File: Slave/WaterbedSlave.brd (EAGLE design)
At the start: 53.2 x 50.4 mm, 8 parts

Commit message: Update WaterbedSlave.brd
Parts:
- added LED1: (no value), led:CHIPLED_0805
- added R1: 330, SparkFun-Resistors:0805
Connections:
- new net N$10: LED1.A, R1.1
- net GND: now also LED1.C
- net N$16: now also R1.2
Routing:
- net N$16: track 17.7 -> 21.1 mm
- net N$10: track 0.00 -> 2.45 mm
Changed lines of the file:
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@@
 <wire x1="0.2" y1="49.8" x2="0.4" y2="50" width="0.3048" layer="21"/>
 <text x="25.46" y="5.83" size="1.9304" layer="21" font="vector" ratio="13">Heat Pad</text>
-<text x="9.8" y="10.5" size="2.1844" layer="22" font="vector" ratio="13" rot="MR90">CuriousTech.net</text>
+<text x="8" y="11.2" size="2.1844" layer="22" font="vector" ratio="13" rot="MR90">CuriousTech.net</text>
 <text x="3" y="1.4" size="2.1844" layer="22" font="vector" ratio="13" rot="MR90">WiFi Waterbed Heater Slave</text>
 <text x="36.2" y="42.3" size="1.016" layer="21" font="vector" ratio="13">G 3v3 S</text>
@@
 <element name="JP2" library="SparkFun-Connectors" package="1X01_2MM" value="" x="38.4" y="3.9" rot="R180"/>
 <element name="F1" library="SparkFun-Capacitors" package="CAP-PTH-5MM" value="" x="22" y="14.3" rot="R90"/>
+<element name="LED1" library="led" package="CHIPLED_0805" value="" x="49.9" y="47.9" rot="R270"/>
+<element name="R1" library="SparkFun-Resistors" package="0805" value="330" x="45.6" y="47.8" rot="R180"/>
 </elements>
 <signals>
@@
 <contactref element="C1" pad="-"/>
 <contactref element="SUPP" pad="3V3"/>
+<contactref element="LED1" pad="C"/>
 </signal>
 <signal name="N$9">
@@
 <wire x1="48.268" y1="34.19" x2="49.586" y2="34.19" width="1.016" layer="1"/>
 <wire x1="49.586" y1="34.19" x2="49.134" y2="34.142" width="1.016" layer="1"/>
+<contactref element="R1" pad="2"/>
+<wire x1="44.7" y1="47.8" x2="41.812" y2="47.8" width="0.4064" layer="1"/>
+<wire x1="41.812" y1="47.8" x2="41.812" y2="47.333" width="0.4064" layer="1"/>
 </signal>
 <signal name="N$13">
@@
 <wire x1="27.68" y1="11.12" x2="22" y2="16.8" width="1.27" layer="1"/>
 </signal>
+<signal name="N$10">
+<contactref element="R1" pad="1"/>
+<contactref element="LED1" pad="A"/>
+<wire x1="46.5" y1="47.8" x2="48.85" y2="47.8" width="0.4064" layer="1"/>
+<wire x1="48.85" y1="47.8" x2="48.85" y2="47.9" width="0.4064" layer="1"/>
+</signal>
 </signals>

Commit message: New cheap model
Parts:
- removed C1: 330uF, resistor:TT5D9
- removed JP2, JP3: (no value), SparkFun-Connectors:1X01_2MM
- removed LED1: (no value), led:CHIPLED_0805
- removed SUPP: RAC02-3.3SC, CuriousTech:RAC02-3.3SC
- added LED: (no value), led:CHIPLED_0805
- added O1, O2: (no value), SparkFun-Connectors:1X01_2MM
- added R2: 330, SparkFun-Resistors:0805
- added SSR: IXYS CPC1998J, CuriousTech:I4-PAC
- U$2: value SSR-5A-240VAC -> 3V3AC-DC; device CuriousTech:SIP-4 -> CuriousTech:ACDC33
- moved JP1 45.8 mm to (28.5, 2.11), turned to 90 degrees
- moved R1 42.7 mm to (33.0, 7.00), turned to 90 degrees
- moved F1 35.6 mm to (12.3, 48.6), turned to 0 degrees
- moved U$2 25.0 mm to (25.1, 32.3)
- moved U$3 5.40 mm to (2.50, 25.3)
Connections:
- removed net N$14: SUPP.AC2, U$2.P$3, U$3.H
- new net N$2: F1.2, U$2.AC2
- new net N$3: O2.1, SSR.P$3
- net GND: now also LED.C, SSR.P$1, U$2.3V3; no longer C1.-, LED1.C, SUPP.3V3, U$2.P$1
- net N$1: now also O1.1, U$2.AC1; no longer F1.1, JP3.1
- net N$10: now also LED.A; no longer LED1.A
- net N$15: now also U$2.GND; no longer C1.+, SUPP.GND
- net N$16: now also R2.1; no longer U$2.P$2
- net N$5: now also R2.2, SSR.P$2; no longer F1.2, SUPP.AC1
- net N$6: now also F1.1, SSR.P$4, U$3.H; no longer JP2.1, U$2.P$4
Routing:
- net N$6: track 15.8 -> 68.6 mm
- net N$14: track 48.7 -> 0.00 mm
- net N$2: track 37.2 -> 5.47 mm
- net N$1: track 36.2 -> 53.4 mm
- net N$16: track 21.1 -> 7.63 mm
- net N$3: track 29.5 -> 16.4 mm
- net N$5: track 8.95 -> 2.54 mm
- net N$15: track 20.2 -> 18.2 mm
- removed copper zone on layer 16, net GND
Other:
- board size 53.2 x 50.4 mm -> 36 x 50.3 mm
- board text added: "+"
- board text added: "-"
- board text added: "AC"
- board text removed: "600W max"
- board text removed: "Heat Pad"

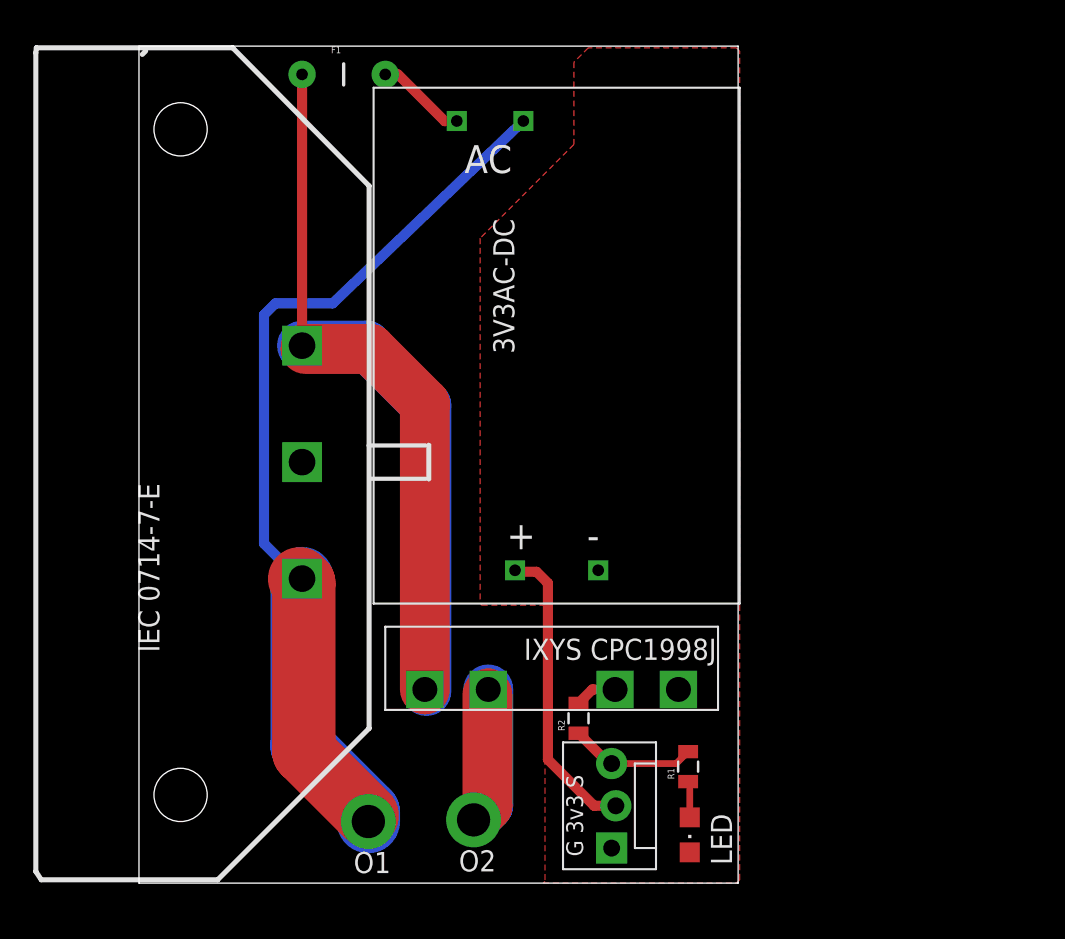
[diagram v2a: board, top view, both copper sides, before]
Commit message: The cheap AC-DC sucked. Using trusted brand.
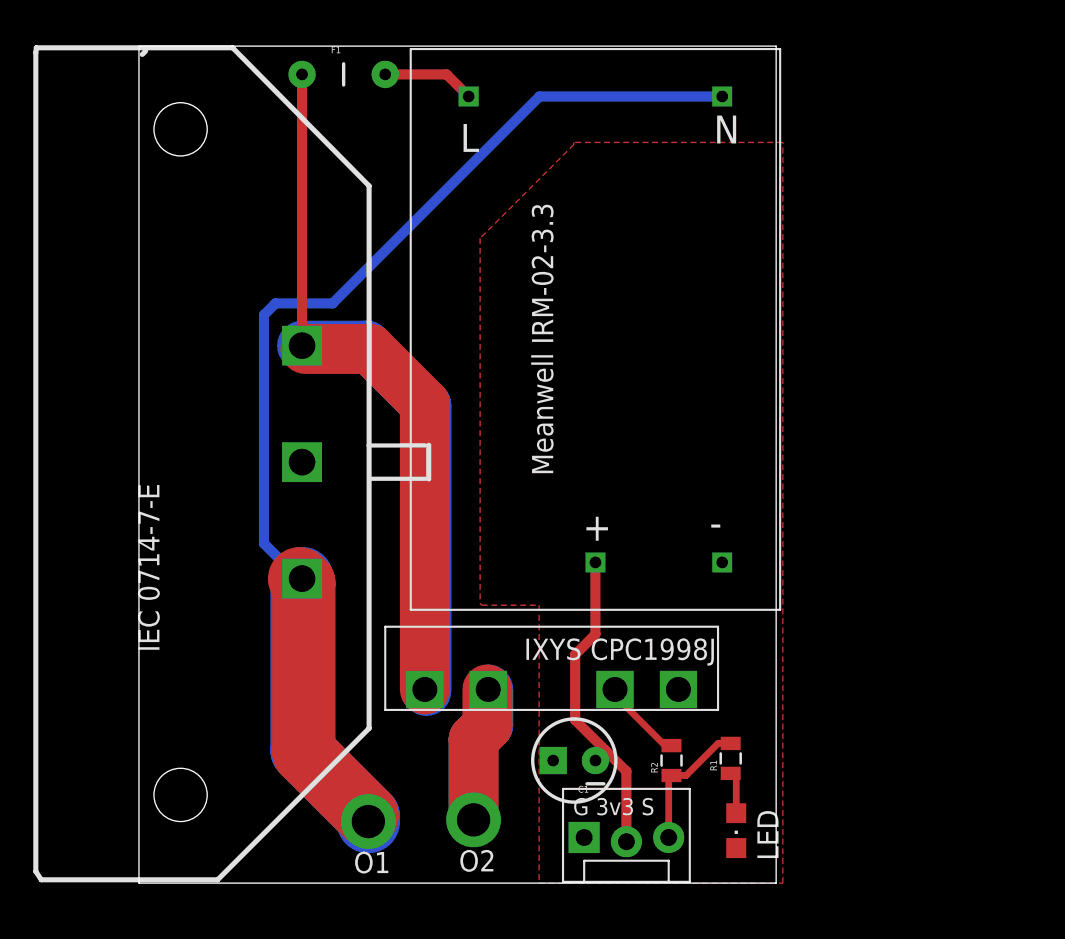
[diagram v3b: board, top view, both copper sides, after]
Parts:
- removed U$2: 3V3AC-DC, CuriousTech:ACDC33
- added C1: 47uF 4V, SparkFun-Capacitors:CPOL-RADIAL-10UF-25V
- added U$1: Meanwell IRM-02-3.3, CuriousTech:RAC02-3.3SC
- moved R2 6.14 mm to (32.0, 7.37)
- moved LED 2.81 mm to (35.9, 3.15)
- moved R1 2.61 mm to (35.6, 7.49)
- moved JP1 1.85 mm to (26.8, 2.61), turned to 0 degrees
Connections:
- net GND: now also C1.1, U$1.3V3; no longer U$2.3V3
- net N$1: now also U$1.AC1; no longer U$2.AC1
- net N$15: now also C1.2, U$1.GND; no longer U$2.GND
- net N$2: now also U$1.AC2; no longer U$2.AC2
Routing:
- net N$1: track 53.4 -> 66.1 mm
- net N$5: track 2.54 -> 5.01 mm
- net N$15: track 18.2 -> 19.4 mm
- net N$16: track 7.63 -> 8.25 mm
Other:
- board size 36 x 50.3 mm -> 38.3 x 50.3 mm
- board text added: "L"
- board text added: "N"
- board text removed: "AC"

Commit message: Simple 10A 3V relay version
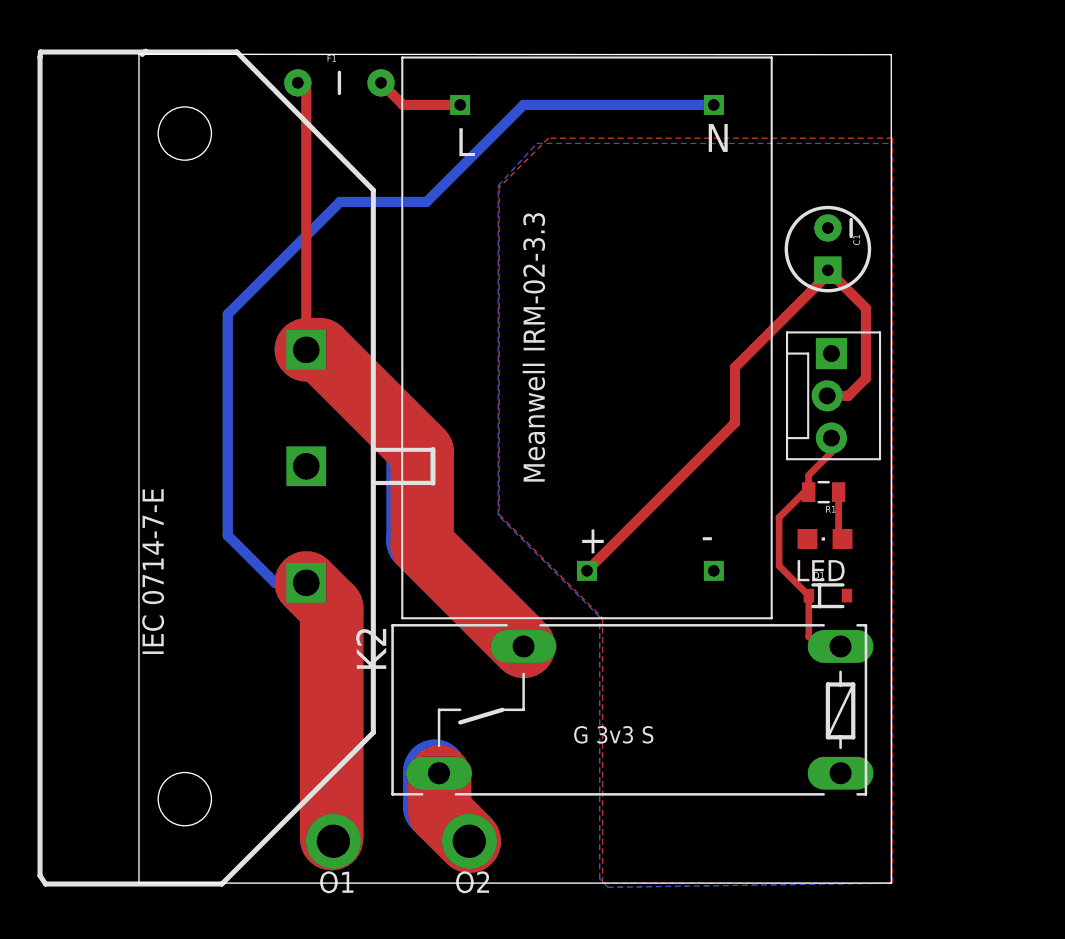
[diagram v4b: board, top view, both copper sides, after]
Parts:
- removed R2: 330, SparkFun-Resistors:0805
- removed SSR: IXYS CPC1998J, CuriousTech:I4-PAC
- added D1: BAT20J, SparkFun-DiscreteSemi:SOD-323
- added K2: G6RS, relay:G6RS
- moved C1 34.3 mm to (41.4, 38.1), turned to 270 degrees
- moved JP1 32.7 mm to (41.5, 31.8), turned to 270 degrees
- moved LED 18.3 mm to (41.2, 20.7), turned to 90 degrees
- moved R1 16.9 mm to (41.1, 23.5), turned to 180 degrees
- moved O1 2.41 mm to (11.7, 2.51)
- moved O2 1.31 mm to (19.9, 2.51)
- moved U$1 0.72 mm to (26.9, 32.8)
- moved F1 0.57 mm to (12.0, 48.1)
- moved U$3 0.36 mm to (2.75, 25.0)
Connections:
- removed net N$15: C1.2, JP1.2, U$1.GND
- removed net N$5: R2.2, SSR.P$2
- removed net N$6: F1.1, SSR.P$4, U$3.H
- new net 3V3: C1.1, JP1.2, U$1.GND
- new net N$4: F1.1, K2.P, U$3.H
- net GND: now also C1.2, D1.A, K2.2; no longer C1.1, SSR.P$1
- net N$16: now also D1.C, K2.1; no longer R2.1
- net N$3: now also K2.S; no longer SSR.P$3
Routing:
- net N$6: track 68.6 -> 0.00 mm
- net N$4: track 15.9 -> 63.7 mm
- net 3V3: track 0.00 -> 34.3 mm
- net N$1: track 66.1 -> 85.9 mm
- net N$15: track 19.4 -> 0.00 mm
- net N$16: track 8.25 -> 16.3 mm
- net N$3: track 16.4 -> 9.67 mm
- net N$5: track 5.01 -> 0.00 mm
- added copper zone on layer 16, net GND
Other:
- board size 38.3 x 50.3 mm -> 45.2 x 49.8 mm
